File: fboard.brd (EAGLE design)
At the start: 60.9 x 51.7 mm, 29 parts, among them Q1 SL2305, U1 ATMEGA328PB-AU, U2 MPU-6050, U3 SN74HC138PW

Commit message: added easter egg
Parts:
- moved C6 0.25 mm to (46.0, 43.2)
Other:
- board text added: "C:/Users/Michael/Desktop/lenny.bmp"

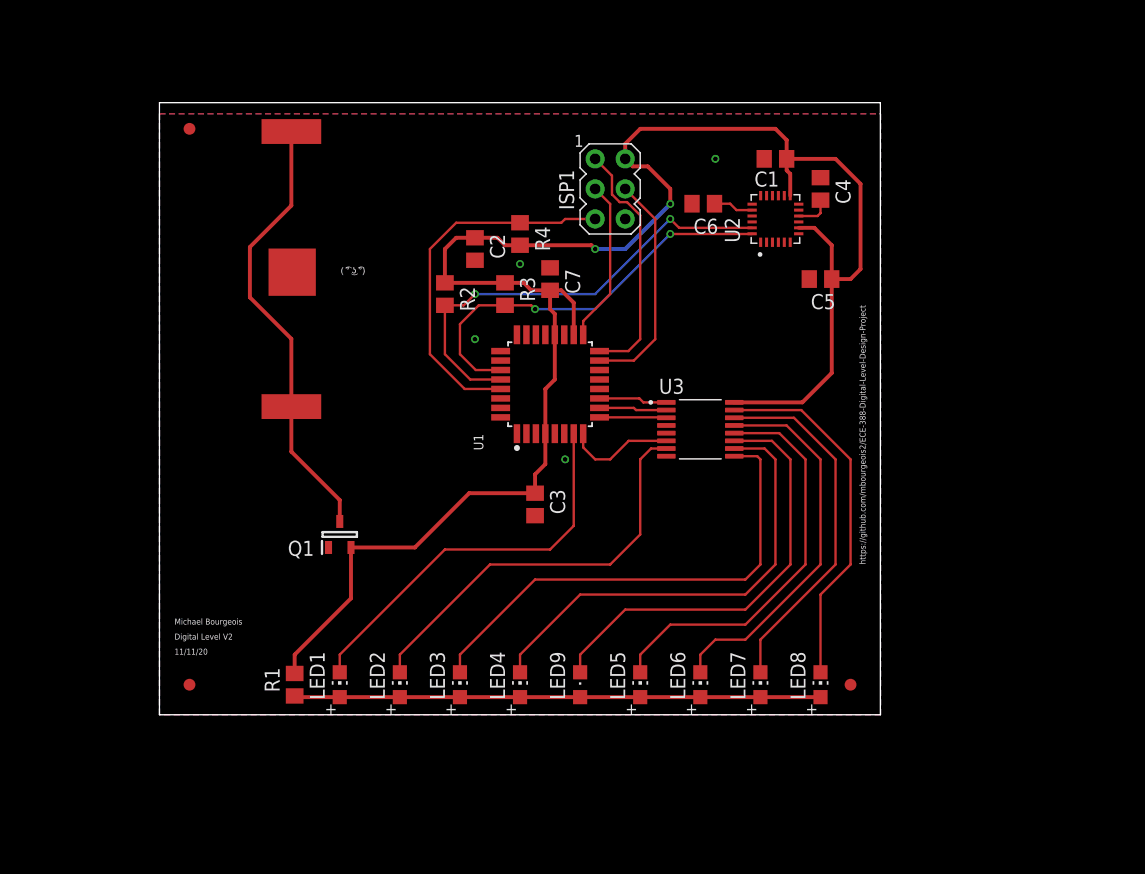
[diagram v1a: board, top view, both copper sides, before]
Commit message: bigger font and power traces are 12mil
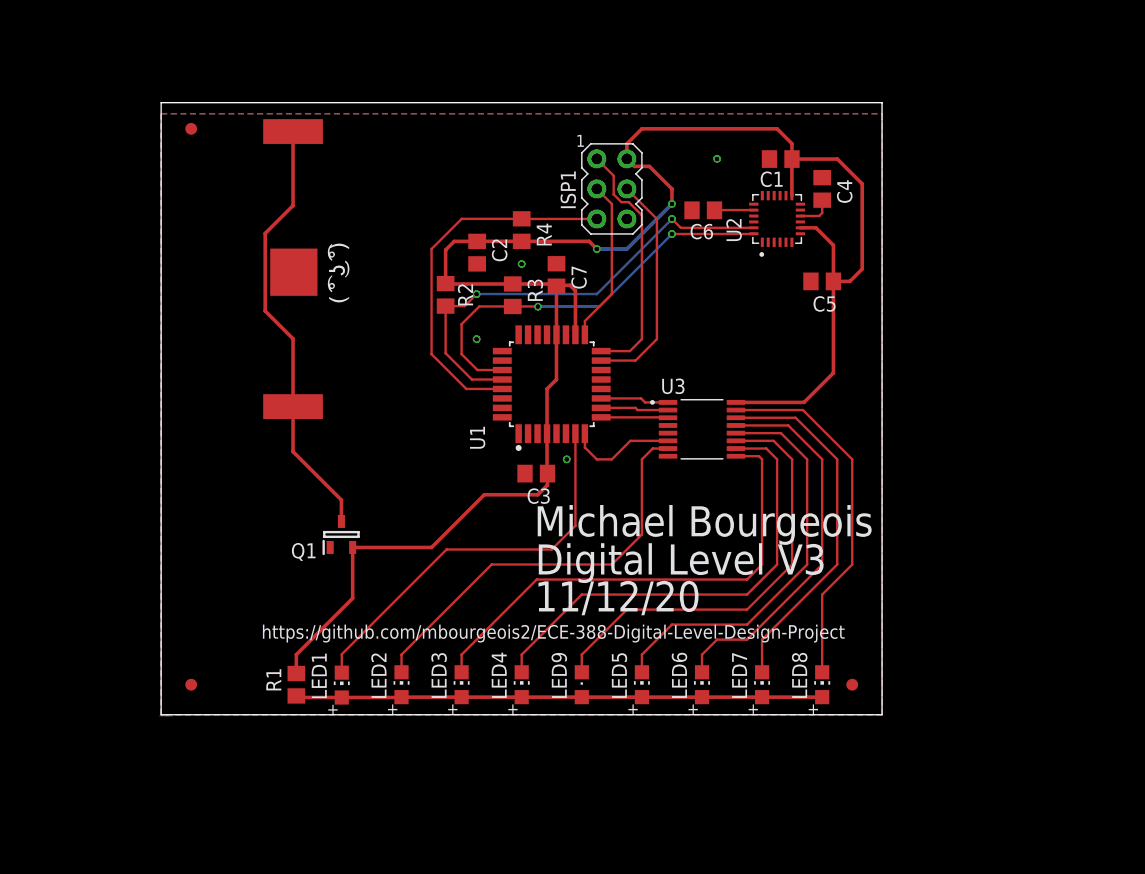
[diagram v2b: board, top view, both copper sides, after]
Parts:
- moved C3 2.61 mm to (31.9, 20.4), turned to 180 degrees
- moved R3 0.66 mm to (29.9, 35.5)
- moved C7 0.64 mm to (33.6, 37.2)
- moved C6 0.56 mm to (46.0, 42.6)
- moved C1 0.45 mm to (52.5, 47.0)
- moved R4 0.36 mm to (30.6, 41.0)
- moved C2 0.36 mm to (26.9, 39.1)
- moved C5 0.24 mm to (56.0, 36.6)
- moved LED1 0.18 mm to (15.4, 2.51)
- moved LED3 0.14 mm to (25.5, 2.54)
- moved U$5 0.14 mm to (2.68, 49.5)
- moved U$6 0.14 mm to (2.68, 2.54)
- moved BAT1 0.14 mm to (7.76, 48.3)
- moved C4 0.14 mm to (56.0, 44.5)
- moved ISP1 0.14 mm to (38.2, 44.5)
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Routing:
- net N$12: track 37.6 -> 36.6 mm
- net +3V3: track 154.0 -> 154.7 mm
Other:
- board text added: "11/12/20"
- board text added: "Digital Level V3"
- board text removed: "11/11/20"
- board text removed: "Digital Level V2"

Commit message: ground plane?
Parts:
- moved U2 0.28 mm to (52.2, 42.2)
- moved LED1 0.28 mm to (15.4, 2.79)
- moved LED2 0.28 mm to (20.5, 2.82)
- moved LED3 0.28 mm to (25.5, 2.82)
- moved LED4 0.28 mm to (30.6, 2.82)
- moved LED5 0.28 mm to (40.8, 2.82)
- moved LED6 0.28 mm to (45.9, 2.82)
- moved LED7 0.28 mm to (50.9, 2.82)
- moved LED8 0.28 mm to (56.0, 2.82)
- moved LED9 0.28 mm to (35.7, 2.82)
- moved R1 0.28 mm to (11.6, 2.82)
- moved U$4 0.28 mm to (58.6, 2.82)
- moved U$6 0.28 mm to (2.68, 2.82)
- moved BAT1 0.28 mm to (7.76, 48.5)
- moved C1 0.28 mm to (52.5, 47.3)
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
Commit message: fixed airwire
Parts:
- moved C2 0.28 mm to (26.9, 39.6)
- moved U3 0.28 mm to (45.9, 24.7)
- moved Q1 0.28 mm to (15.4, 15.8)
- moved LED1 0.28 mm to (15.4, 3.08)
- moved LED2 0.28 mm to (20.5, 3.11)
- moved LED3 0.28 mm to (25.5, 3.11)
- moved LED4 0.28 mm to (30.6, 3.11)
- moved LED5 0.28 mm to (40.8, 3.11)
- moved LED6 0.28 mm to (45.9, 3.11)
- moved LED7 0.28 mm to (50.9, 3.11)
- moved LED8 0.28 mm to (56.0, 3.11)
- moved LED9 0.28 mm to (35.7, 3.11)
- moved R1 0.28 mm to (11.6, 3.11)
- moved U$4 0.28 mm to (58.6, 3.11)
- moved U$6 0.28 mm to (2.68, 3.11)
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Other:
- board text removed: "C:/Users/Michael/Desktop/lenny.bmp"

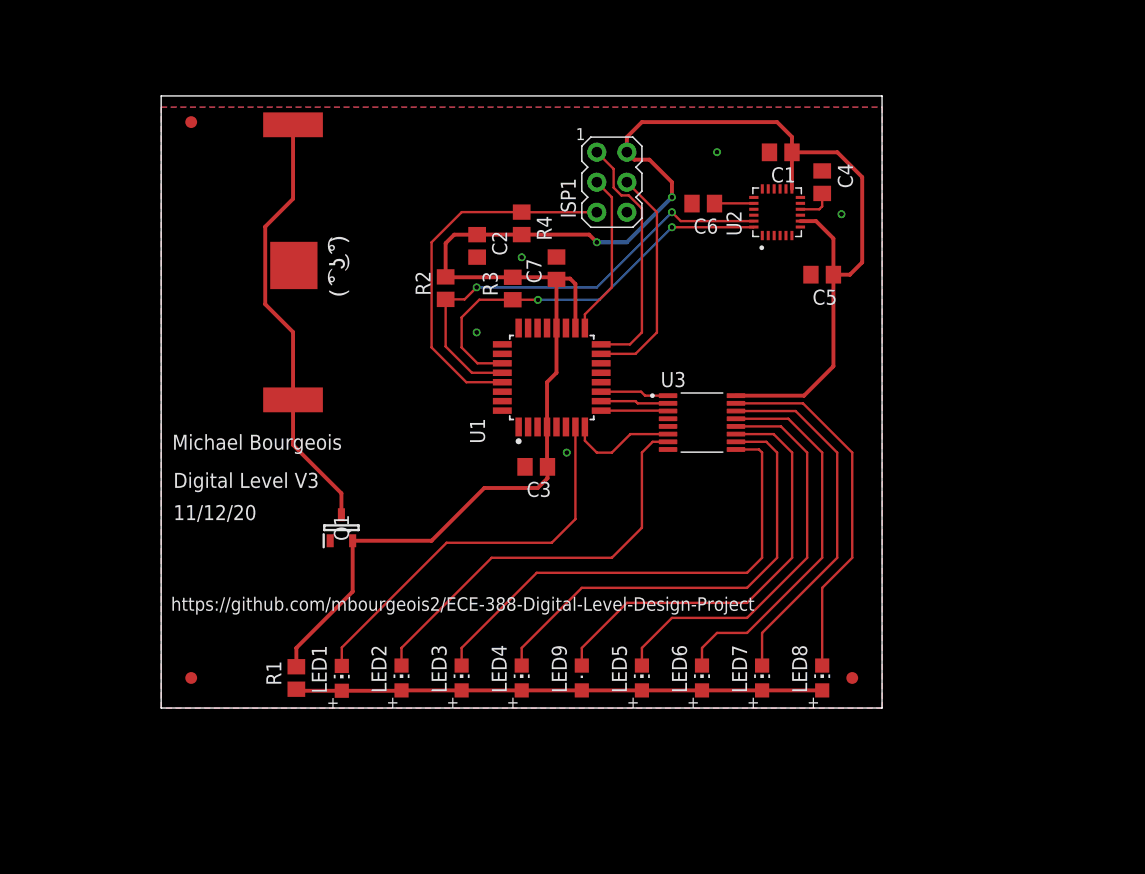
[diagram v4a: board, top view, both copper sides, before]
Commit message: redid ground plane
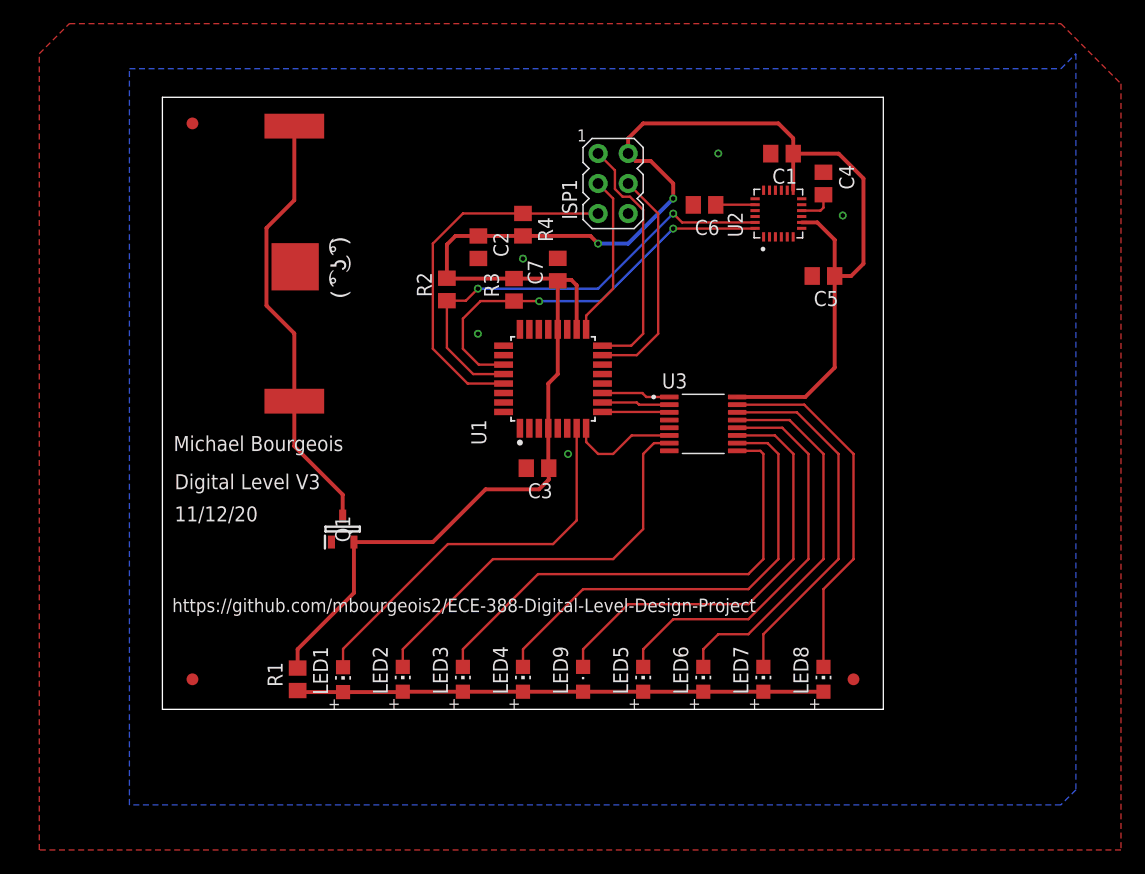
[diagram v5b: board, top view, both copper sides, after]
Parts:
- moved C2 0.15 mm to (27.0, 39.5)
- moved ISP1 0.15 mm to (38.3, 44.9)
- moved U2 0.15 mm to (52.3, 42.4)
- moved R2 0.15 mm to (24.3, 36.0)
- moved U3 0.15 mm to (46.0, 24.6)
- moved LED2 0.15 mm to (20.6, 3.00)
- moved LED5 0.15 mm to (40.9, 3.00)
- moved LED6 0.15 mm to (46.0, 3.00)
- moved LED7 0.15 mm to (51.0, 3.00)
- moved U$4 0.15 mm to (58.7, 3.00)
- moved Q1 0.15 mm to (15.5, 15.7)
- moved R1 0.15 mm to (11.7, 3.00)
- moved U$6 0.15 mm to (2.79, 3.00)
- moved C4 0.15 mm to (56.1, 44.9)
- moved C1 0.15 mm to (52.6, 47.4)
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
